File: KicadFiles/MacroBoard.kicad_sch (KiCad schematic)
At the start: 79 parts, among them J1 USB_B_Micro, J2 Conn_01x08_Male, SW1 SW_Push, SW10 SW_Push, SW11 SW_Push, SW12 SW_Push, SW13 SW_Push, SW14 SW_Push, SW15 SW_Push, SW16 SW_Push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

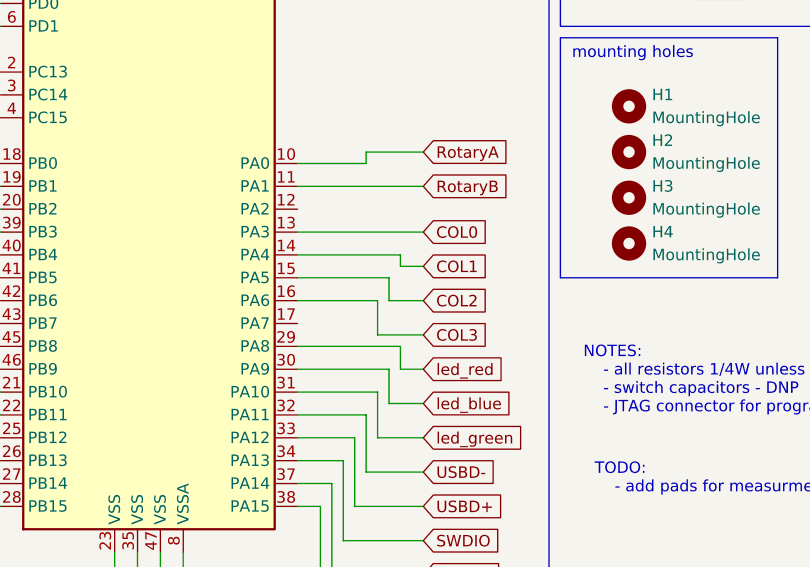
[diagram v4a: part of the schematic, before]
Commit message: flipped columns, connected columns and rows and programming pins in pcb
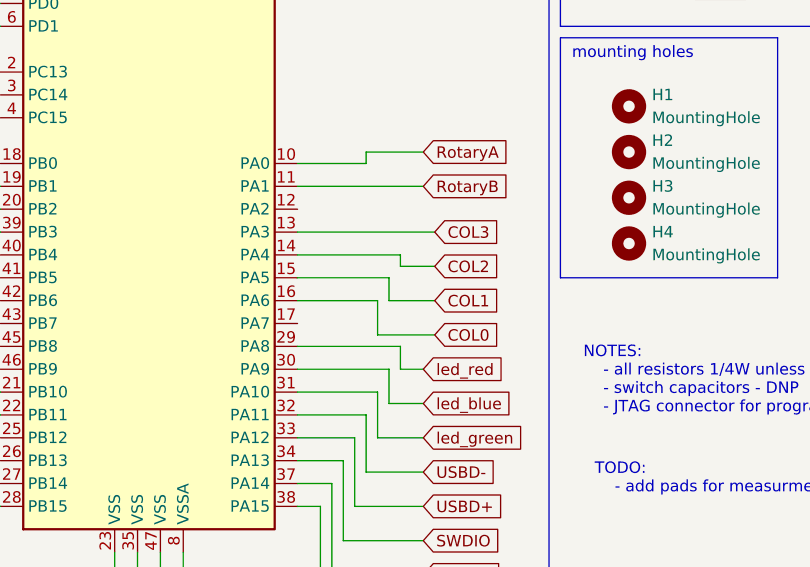
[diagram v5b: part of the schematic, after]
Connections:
- net COL0: now also U1.16 (PA6); no longer U1.13 (PA3)
- net COL1: now also U1.15 (PA5); no longer U1.14 (PA4)
- net COL2: now also U1.14 (PA4); no longer U1.15 (PA5)
- net COL3: now also U1.13 (PA3); no longer U1.16 (PA6)
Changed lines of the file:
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@@
-    (stroke (width 0) (type default) (color 0 0 0 0))
-  )
-  (wire (pts (xy 207.01 111.76) (xy 209.55 111.76))
     (stroke (width 0) (type default) (color 0 0 0 0))
   )
@@
     (stroke (width 0) (type default) (color 0 0 0 0))
   )
-  (wire (pts (xy 204.47 119.38) (xy 209.55 119.38))
-    (stroke (width 0) (type default) (color 0 0 0 0))
-  )
   (wire (pts (xy 82.55 71.12) (xy 85.09 71.12))
     (stroke (width 0) (type default) (color 0 0 0 0))
@@
     (stroke (width 0) (type default) (color 0 0 0 0))
   )
+  (wire (pts (xy 207.01 111.76) (xy 210.82 111.76))
+    (stroke (width 0) (type default) (color 0 0 0 0))
+  )
   (wire (pts (xy 229.87 44.45) (xy 229.87 41.91))
     (stroke (width 0) (type default) (color 0 0 0 0))
@@
     (stroke (width 0) (type default) (color 0 0 0 0))
   )
-  (wire (pts (xy 205.74 115.57) (xy 209.55 115.57))
-    (stroke (width 0) (type default) (color 0 0 0 0))
-  )
   (wire (pts (xy 38.1 25.4) (xy 38.1 29.21))
     (stroke (width 0) (type default) (color 0 0 0 0))
@@
     (stroke (width 0) (type default) (color 0 0 0 0))
   )
+  (wire (pts (xy 205.74 115.57) (xy 210.82 115.57))
+    (stroke (width 0) (type default) (color 0 0 0 0))
+  )
   (polyline (pts (xy 213.36 13.97) (xy 254 13.97))
     (stroke (width 0) (type default) (color 0 0 0 0))
   )
-  (wire (pts (xy 195.58 107.95) (xy 209.55 107.95))
-    (stroke (width 0) (type default) (color 0 0 0 0))
-  )
   (wire (pts (xy 111.76 111.76) (xy 114.3 111.76))
     (stroke (width 0) (type default) (color 0 0 0 0))
@@
     (stroke (width 0) (type default) (color 0 0 0 0))
   )
+  (wire (pts (xy 204.47 119.38) (xy 210.82 119.38))
+    (stroke (width 0) (type default) (color 0 0 0 0))
+  )
   (polyline (pts (xy 111.76 83.82) (xy 60.96 83.82))
     (stroke (width 0) (type default) (color 0 0 0 0))
@@
   )
   (wire (pts (xy 111.76 134.62) (xy 111.76 130.81))
+    (stroke (width 0) (type default) (color 0 0 0 0))
+  )
+  (wire (pts (xy 195.58 107.95) (xy 210.82 107.95))
     (stroke (width 0) (type default) (color 0 0 0 0))
   )
@@
     )
   )
-  (global_label "COL1" (shape input) (at 209.55 111.76 0) (fields_autoplaced)
-    (effects (font (size 1.27 1.27)) (justify left))
-    (property "Intersheet References" "${INTERSHEET_REFS}" (id 0) (at 216.8012 111.6806 0)
+  (global_label "COL1" (shape input) (at 210.82 115.57 0) (fields_autoplaced)
+    (effects (font (size 1.27 1.27)) (justify left))
+    (property "Intersheet References" "${INTERSHEET_REFS}" (id 0) (at 218.0712 115.4906 0)
       (effects (font (size 1.27 1.27)) (justify left) hide)
     )
@@
     )
   )
-  (global_label "COL0" (shape input) (at 209.55 107.95 0) (fields_autoplaced)
-    (effects (font (size 1.27 1.27)) (justify left))
-    (property "Intersheet References" "${INTERSHEET_REFS}" (id 0) (at 216.8012 107.8706 0)
+  (global_label "COL0" (shape input) (at 210.82 119.38 0) (fields_autoplaced)
+    (effects (font (size 1.27 1.27)) (justify left))
+    (property "Intersheet References" "${INTERSHEET_REFS}" (id 0) (at 218.0712 119.3006 0)
       (effects (font (size 1.27 1.27)) (justify left) hide)
     )
@@
     )
   )
-  (global_label "COL3" (shape input) (at 209.55 119.38 0) (fields_autoplaced)
-    (effects (font (size 1.27 1.27)) (justify left))
-    (property "Intersheet References" "${INTERSHEET_REFS}" (id 0) (at 216.8012 119.3006 0)
+  (global_label "COL3" (shape input) (at 210.82 107.95 0) (fields_autoplaced)
+    (effects (font (size 1.27 1.27)) (justify left))
+    (property "Intersheet References" "${INTERSHEET_REFS}" (id 0) (at 218.0712 107.8706 0)
       (effects (font (size 1.27 1.27)) (justify left) hide)
     )
@@
     )
   )
-  (global_label "COL2" (shape input) (at 209.55 115.57 0) (fields_autoplaced)
-    (effects (font (size 1.27 1.27)) (justify left))
-    (property "Intersheet References" "${INTERSHEET_REFS}" (id 0) (at 216.8012 115.4906 0)
-      (effects (font (size 1.27 1.27)) (justify left) hide)
-    )
+  (global_label "COL2" (shape input) (at 210.82 111.76 0) (fields_autoplaced)
+    (effects (font (size 1.27 1.27)) (justify left))
+    (property "Intersheet References" "${INTERSHEET_REFS}" (id 0) (at 218.0712 111.6806 0)
+      (effects (font (size 1.27 1.27)) (justify left) hide)
+    )
